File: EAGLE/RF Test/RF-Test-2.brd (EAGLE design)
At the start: 20.3 x 35.6 mm, 8 parts, among them X1 SMA-142-0701-881/886, X2 IPEX-20279-001E

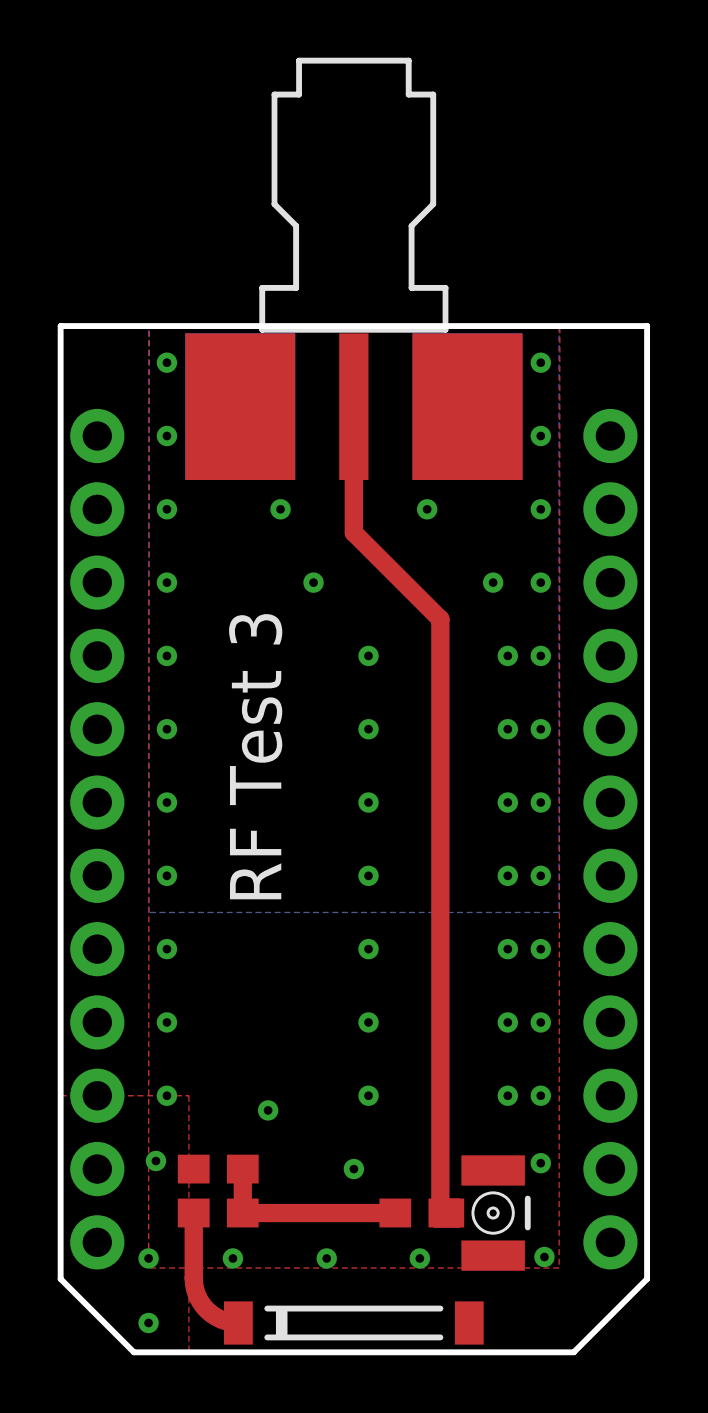
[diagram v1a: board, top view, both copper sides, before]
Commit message: Reduce stripline length, shorten test board.
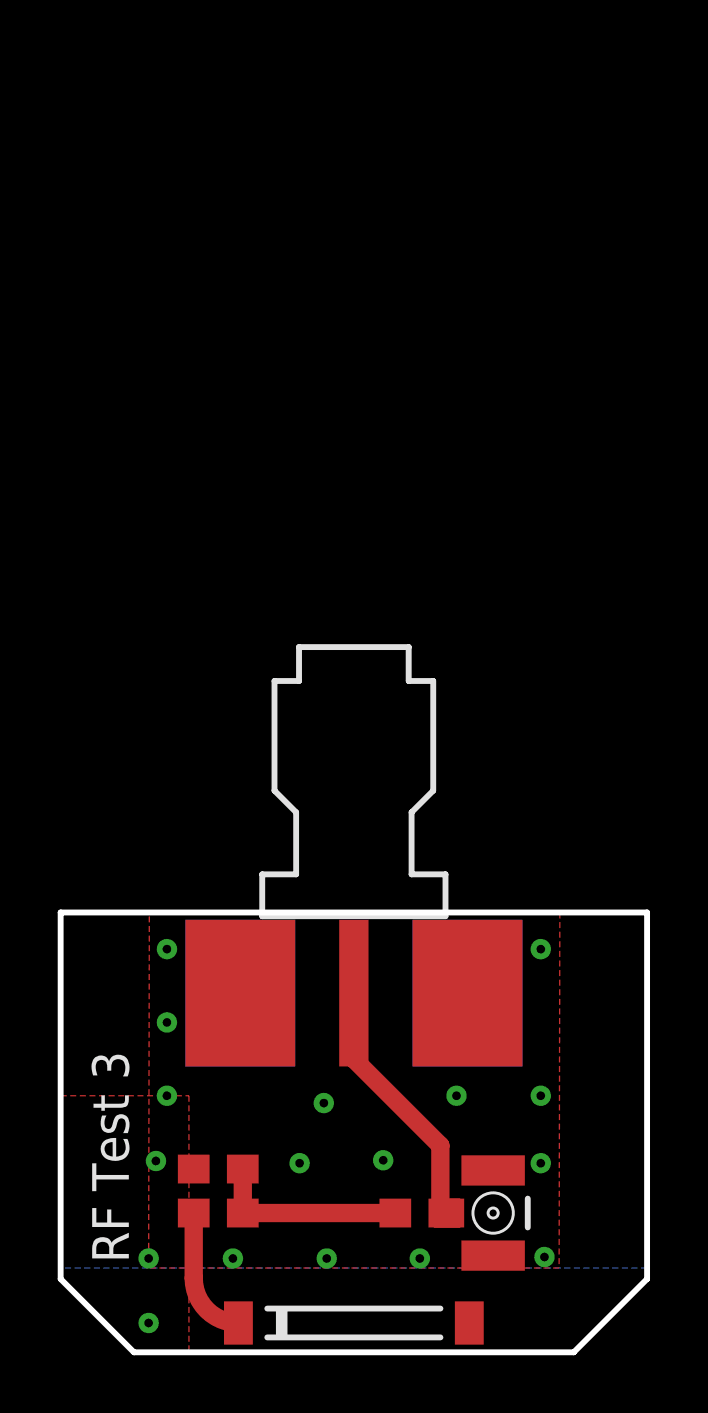
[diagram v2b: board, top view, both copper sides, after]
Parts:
- removed JP1, JP2: (no value), SparkFun:1X12
- moved X1 20.3 mm to (10.2, 12.5)
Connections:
- removed net !RST: JP2.2
- removed net +3V3: JP2.1
- removed net A0: JP1.12
- removed net A1: JP1.11
- removed net A2: JP1.10
- removed net A3: JP1.9
- removed net A4: JP1.8
- removed net A5: JP1.7
- removed net A6: JP1.6
- removed net A7: JP1.5
- removed net D0: JP2.12
- removed net D1: JP2.11
- removed net D2: JP2.10
- removed net D3: JP2.9
- removed net D4: JP2.8
- removed net D5: JP2.7
- removed net D6: JP2.6
- removed net D7: JP2.5
- removed net RAW: JP1.1
- removed net RX: JP1.4
- removed net TX: JP1.3
- removed net VDDA: JP2.3
- net GND: no longer JP1.2, JP2.4
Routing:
- net N$4: track 29.2 -> 8.92 mm
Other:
- board size 20.3 x 35.6 mm -> 20.3 x 15.2 mm
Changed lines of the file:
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@@
 <board>
 <plain>
-<wire x1="0" y1="33.02" x2="0" y2="0" width="0.2032" layer="20"/>
+<wire x1="0" y1="12.7" x2="0" y2="0" width="0.2032" layer="20"/>
 <wire x1="0" y1="0" x2="2.54" y2="-2.54" width="0.2032" layer="20"/>
 <wire x1="2.54" y1="-2.54" x2="17.78" y2="-2.54" width="0.2032" layer="20"/>
 <wire x1="17.78" y1="-2.54" x2="20.32" y2="0" width="0.2032" layer="20"/>
-<wire x1="20.32" y1="0" x2="20.32" y2="33.02" width="0.2032" layer="20"/>
-<wire x1="20.32" y1="33.02" x2="0" y2="33.02" width="0.2032" layer="20"/>
-<wire x1="17.78" y1="0.508" x2="17.78" y2="29.21" width="0.2032" layer="51"/>
-<wire x1="2.54" y1="0.508" x2="2.54" y2="29.21" width="0.2032" layer="51"/>
-<text x="5.8674" y="23.2156" size="1.778" layer="21" rot="R270">RF Test 3</text>
+<wire x1="20.32" y1="0" x2="20.32" y2="12.7" width="0.2032" layer="20"/>
+<wire x1="20.32" y1="12.7" x2="0" y2="12.7" width="0.2032" layer="20"/>
+<text x="2.3622" y="0.5588" size="1.27" layer="21" rot="R90">RF Test 3</text>
 </plain>
 <attributes>
@@
 </autorouter>
 <elements>
-<element name="JP1" library="SparkFun" package="1X12" value="" x="1.27" y="29.21" locked="yes" rot="MR270"/>
-<element name="JP2" library="SparkFun" package="1X12" value="" x="19.05" y="29.21" locked="yes" rot="MR270"/>
 <element name="L1" library="SparkFun-Passives" package="0603" value="2.2nH" x="5.461" y="3.81" smashed="yes" rot="R180">
 <attribute name="VALUE" x="9.525" y="4.064" size="0.6096" layer="27" font="vector" rot="R180"/>
@@
 <attribute name="VALUE" x="11.811" y="0.381" size="1.27" layer="27"/>
 </element>
-<element name="X1" library="andyw-oct-2011" package="ANDYW-GENERIC-END-LAUNCH" value="SMA-142-0701-881/886" x="10.16" y="32.7914" smashed="yes" rot="R270">
-<attribute name="OC_NEWARK" value="08B906" x="10.16" y="32.7914" size="1.778" layer="27" rot="R270" display="off"/>
-<attribute name="MPN" value="142-0701-881" x="10.16" y="32.7914" size="1.778" layer="27" rot="R270" display="off"/>
-<attribute name="MF" value="JOHNSON COMPONENTS" x="10.16" y="32.7914" size="1.778" layer="27" rot="R270" display="off"/>
-<attribute name="OC_FARNELL" value="1608603" x="10.16" y="32.7914" size="1.778" layer="27" rot="R270" display="off"/>
-<attribute name="VALUE" x="1.27" y="31.5214" size="1.778" layer="27" rot="R270"/>
+<element name="X1" library="andyw-oct-2011" package="ANDYW-GENERIC-END-LAUNCH" value="SMA-142-0701-881/886" x="10.16" y="12.4714" smashed="yes" rot="R270">
+<attribute name="OC_NEWARK" value="08B906" x="10.16" y="12.4714" size="1.778" layer="27" rot="R270" display="off"/>
+<attribute name="MPN" value="142-0701-881" x="10.16" y="12.4714" size="1.778" layer="27" rot="R270" display="off"/>
+<attribute name="MF" value="JOHNSON COMPONENTS" x="10.16" y="12.4714" size="1.778" layer="27" rot="R270" display="off"/>
+<attribute name="OC_FARNELL" value="1608603" x="10.16" y="12.4714" size="1.778" layer="27" rot="R270" display="off"/>
+<attribute name="VALUE" x="1.27" y="11.2014" size="1.778" layer="27" rot="R270"/>
 </element>
 </elements>
@@
 <signal name="GND" class="1">
 <contactref element="L1" pad="2"/>
-<contactref element="JP1" pad="2"/>
-<contactref element="JP2" pad="4"/>
 <polygon width="0.2032" layer="2" isolate="0.2032">
-<vertex x="0" y="33.02"/>
-<vertex x="20.32" y="33.02"/>
+<vertex x="0" y="12.7"/>
+<vertex x="20.32" y="12.7"/>
 <vertex x="20.32" y="0.381"/>
 <vertex x="0" y="0.381"/>
@@
 <via x="3.048" y="-1.524" extent="1-16" drill="0.3"/>
 <via x="3.048" y="0.7112" extent="1-16" drill="0.3"/>
-<via x="10.16" y="3.81" extent="1-16" drill="0.3"/>
 <polygon width="0.1524" layer="1" thermals="no">
 <vertex x="3.048" y="0.381"/>
-<vertex x="3.0734" y="32.9692"/>
-<vertex x="17.2974" y="32.9692"/>
+<vertex x="3.0734" y="12.7"/>
+<vertex x="17.2974" y="12.7"/>
 <vertex x="17.272" y="0.381"/>
 </polygon>
@@
 <contactref element="X1" pad="G@3"/>
 <contactref element="X1" pad="G@2"/>
-<polygon width="0.1524" layer="16" thermals="no">
-<vertex x="3.048" y="33.02"/>
-<vertex x="17.272" y="33.02"/>
-<vertex x="17.272" y="12.7"/>
-<vertex x="3.048" y="12.7"/>
-</polygon>
-<via x="3.683" y="31.75" extent="1-16" drill="0.3"/>
-<via x="3.683" y="29.21" extent="1-16" drill="0.3"/>
-<via x="3.683" y="26.67" extent="1-16" drill="0.3"/>
-<via x="3.683" y="24.13" extent="1-16" drill="0.3"/>
-<via x="3.683" y="21.59" extent="1-16" drill="0.3"/>
-<via x="3.683" y="19.05" extent="1-16" drill="0.3"/>
-<via x="3.683" y="16.51" extent="1-16" drill="0.3"/>
-<via x="3.683" y="13.97" extent="1-16" drill="0.3"/>
 <via x="3.683" y="11.43" extent="1-16" drill="0.3"/>
 <via x="3.683" y="8.89" extent="1-16" drill="0.3"/>
-<via x="16.637" y="31.75" extent="1-16" drill="0.3"/>
-<via x="7.62" y="26.67" extent="1-16" drill="0.3"/>
-<via x="16.637" y="29.21" extent="1-16" drill="0.3"/>
-<via x="16.637" y="26.67" extent="1-16" drill="0.3"/>
-<via x="16.637" y="24.13" extent="1-16" drill="0.3"/>
-<via x="16.637" y="21.59" extent="1-16" drill="0.3"/>
-<via x="16.637" y="19.05" extent="1-16" drill="0.3"/>
-<via x="16.637" y="16.51" extent="1-16" drill="0.3"/>
-<via x="16.637" y="13.97" extent="1-16" drill="0.3"/>
 <via x="16.637" y="11.43" extent="1-16" drill="0.3"/>
-<via x="16.637" y="8.89" extent="1-16" drill="0.3"/>
 <via x="16.637" y="6.35" extent="1-16" drill="0.3"/>
-<via x="8.763" y="24.13" extent="1-16" drill="0.3"/>
-<via x="10.668" y="21.59" extent="1-16" drill="0.3"/>
-<via x="10.668" y="19.05" extent="1-16" drill="0.3"/>
-<via x="10.668" y="16.51" extent="1-16" drill="0.3"/>
-<via x="10.668" y="13.97" extent="1-16" drill="0.3"/>
-<via x="10.668" y="11.43" extent="1-16" drill="0.3"/>
-<via x="10.668" y="8.89" extent="1-16" drill="0.3"/>
-<via x="10.668" y="6.35" extent="1-16" drill="0.3"/>
-<via x="15.494" y="6.35" extent="1-16" drill="0.3"/>
-<via x="15.494" y="8.89" extent="1-16" drill="0.3"/>
-<via x="15.494" y="11.43" extent="1-16" drill="0.3"/>
-<via x="15.494" y="13.97" extent="1-16" drill="0.3"/>
-<via x="15.494" y="16.51" extent="1-16" drill="0.3"/>
-<via x="15.494" y="19.05" extent="1-16" drill="0.3"/>
-<via x="15.494" y="21.59" extent="1-16" drill="0.3"/>
-<via x="14.986" y="24.13" extent="1-16" drill="0.3"/>
-<via x="12.7" y="26.67" extent="1-16" drill="0.3"/>
+<via x="13.716" y="6.35" extent="1-16" drill="0.3"/>
 <via x="3.683" y="6.35" extent="1-16" drill="0.3"/>
-<via x="7.1882" y="5.842" extent="1-16" drill="0.3"/>
+<via x="9.1186" y="6.096" extent="1-16" drill="0.3"/>
 <polygon width="0.1524" layer="2">
 <vertex x="4.445" y="6.35"/>
@@
 <via x="16.764" y="0.762" extent="1-16" drill="0.3"/>
 <via x="16.637" y="4.0132" extent="1-16" drill="0.3"/>
-</signal>
-<signal name="RAW" class="1">
-<contactref element="JP1" pad="1"/>
-</signal>
-<signal name="+3V3">
-<contactref element="JP2" pad="1"/>
-</signal>
-<signal name="D4">
-<contactref element="JP2" pad="8"/>
-</signal>
-<signal name="D2">
-<contactref element="JP2" pad="10"/>
-</signal>
-<signal name="D0">
-<contactref element="JP2" pad="12"/>
-</signal>
-<signal name="D1">
-<contactref element="JP2" pad="11"/>
-</signal>
-<signal name="D3">
-<contactref element="JP2" pad="9"/>
+<polygon width="0.2032" layer="16" isolate="0.2032">
+<vertex x="0" y="12.7"/>
+<vertex x="20.32" y="12.7"/>
+<vertex x="20.32" y="0.381"/>
+<vertex x="0" y="0.381"/>
+</polygon>
+<via x="11.176" y="4.1148" extent="1-16" drill="0.3"/>
+<via x="8.2804" y="4.0132" extent="1-16" drill="0.3"/>
 </signal>
 <signal name="N$4" class="2">
@@
 <contactref element="X2" pad="1"/>
 <wire x1="13.296" y1="2.286" x2="13.1572" y2="2.4248" width="0.635" layer="1" curve="-90"/>
-<wire x1="13.1572" y1="2.4248" x2="13.1572" y2="22.86" width="0.635" layer="1"/>
-<wire x1="13.1572" y1="22.86" x2="10.16" y2="25.8572" width="0.635" layer="1"/>
-<wire x1="10.16" y1="25.8572" x2="10.16" y2="30.226" width="0.635" layer="1"/>
+<wire x1="13.1572" y1="2.4248" x2="13.1572" y2="4.6228" width="0.635" layer="1"/>
+<wire x1="13.1572" y1="4.6228" x2="10.16" y2="7.62" width="0.635" layer="1"/>
+<wire x1="10.16" y1="7.62" x2="10.16" y2="9.906" width="0.635" layer="1"/>
 <wire x1="13.296" y1="2.286" x2="13.4585" y2="2.286" width="0" layer="19" extent="1-1"/>
 </signal>
-<signal name="!RST">
-<contactref element="JP2" pad="2"/>
-</signal>
-<signal name="A0">
-<contactref element="JP1" pad="12"/>
-</signal>
-<signal name="A1">
-<contactref element="JP1" pad="11"/>
-</signal>
-<signal name="TX">
-<contactref element="JP1" pad="3"/>
-</signal>
-<signal name="RX">
-<contactref element="JP1" pad="4"/>
-</signal>
-<signal name="A2">
-<contactref element="JP1" pad="10"/>
-</signal>
-<signal name="A3">
-<contactref element="JP1" pad="9"/>
-</signal>
-<signal name="A4">
-<contactref element="JP1" pad="8"/>
-</signal>
-<signal name="A5">
-<contactref element="JP1" pad="7"/>
-</signal>
-<signal name="A6">
-<contactref element="JP1" pad="6"/>
-</signal>
-<signal name="A7">
-<contactref element="JP1" pad="5"/>
-</signal>
-<signal name="D5">
-<contactref element="JP2" pad="7"/>
-</signal>
-<signal name="D6">
-<contactref element="JP2" pad="6"/>
-</signal>
-<signal name="D7">
-<contactref element="JP2" pad="5"/>
-</signal>
-<signal name="VDDA">
-<contactref element="JP2" pad="3"/>
-</signal>
 <signal name="N$3" class="2">
